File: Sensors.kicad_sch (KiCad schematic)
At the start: 7 parts, among them U1 ICM-42670-P, U401 MPU-6050

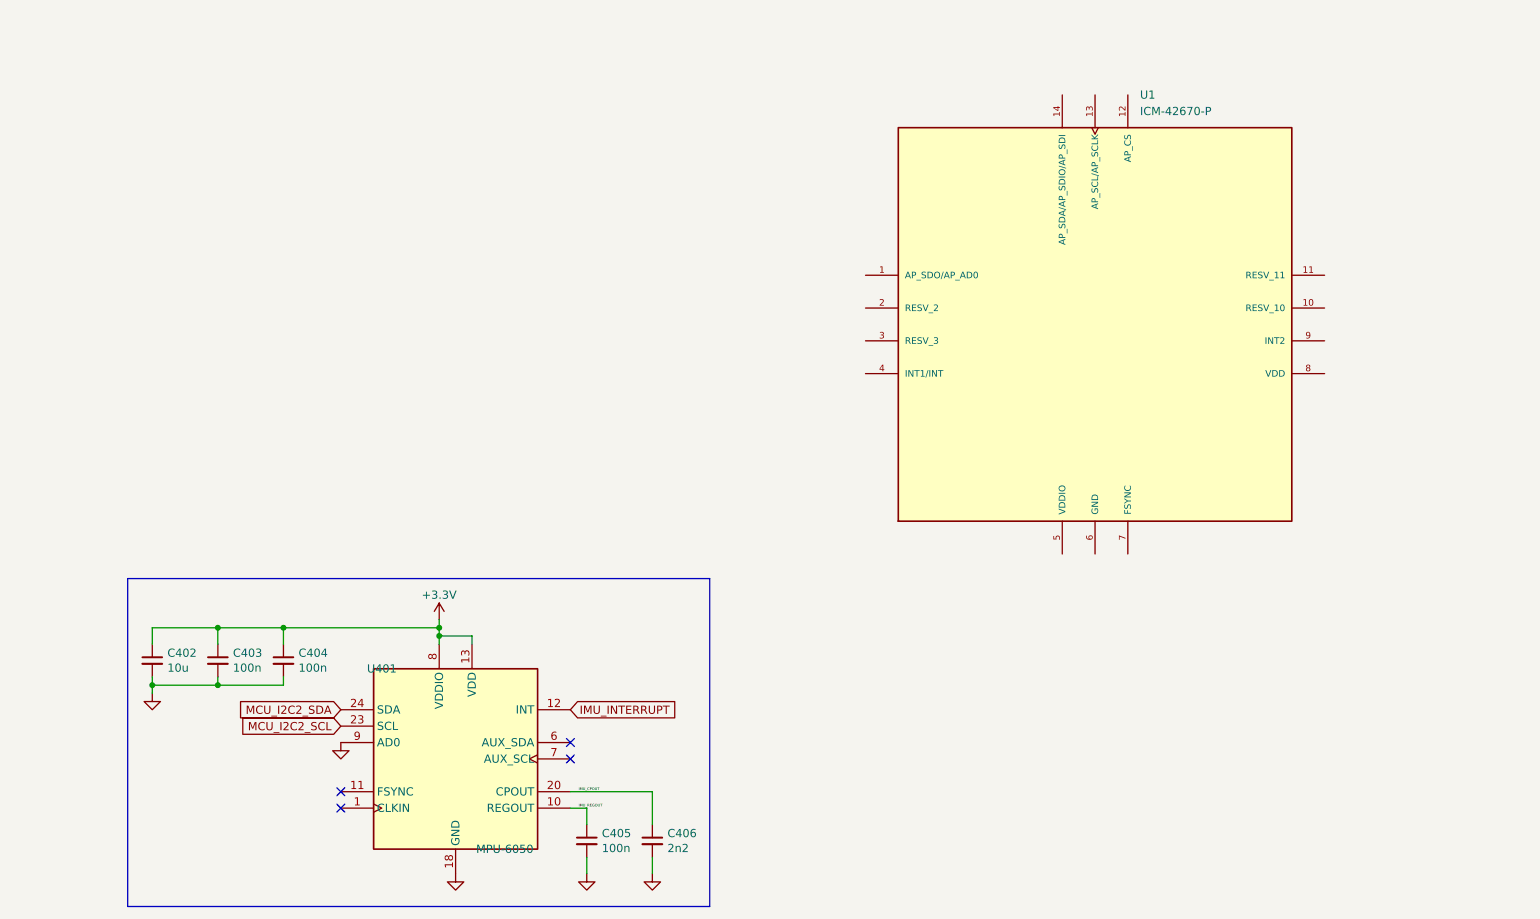
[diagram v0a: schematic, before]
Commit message: replaced CAN transceiver, introduced new IMU
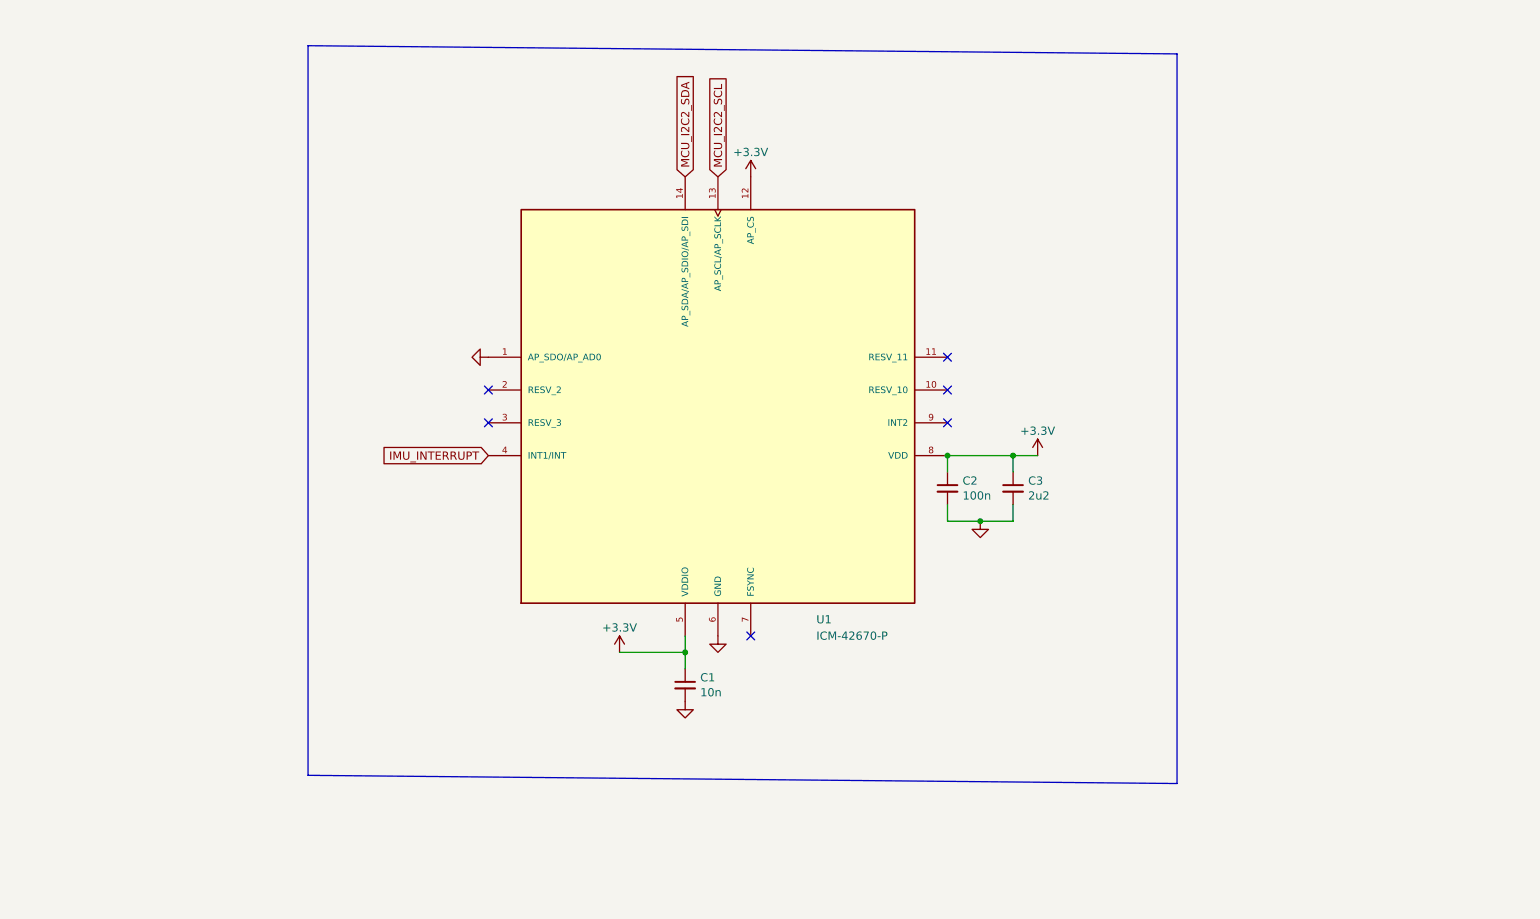
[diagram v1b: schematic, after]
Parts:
- removed C402: 10u, Capacitor_SMD:C_0603_1608Metric, symbol Device:C_Small
- removed C403, C404, C405: 100n, Capacitor_SMD:C_0402_1005Metric, symbol Device:C_Small
- removed C406: 2n2, Capacitor_SMD:C_0402_1005Metric, symbol Device:C_Small
- removed U401: MPU-6050, Sensor_Motion:InvenSense_QFN-24_4x4mm_P0.5mm, symbol Sensor_Motion:MPU-6050
- added C1: 10n, Capacitor_SMD:C_0402_1005Metric, symbol Device:C_Small
- added C2: 100n, Capacitor_SMD:C_0402_1005Metric, symbol Device:C_Small
- added C3: 2u2, Capacitor_SMD:C_0402_1005Metric, symbol Device:C_Small
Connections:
- net +3V3: now also U1.12 (AP_CS), U1.5 (VDDIO), U1.8 (VDD), C1.1, C2.1, C3.1
- net GND: now also U1.1 (AP_SDO/AP_AD0), U1.6 (GND), C1.2, C2.2, C3.2
- net IMU_INTERRUPT: now also U1.4 (INT1/INT)
- net MCU_I2C2_SCL: now also U1.13 (AP_SCL/AP_SCLK)
- net MCU_I2C2_SDA: now also U1.14 (AP_SDA/AP_SDIO/AP_SDI)
- no-connect marks 4 -> 6
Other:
- moved on the sheet: U1

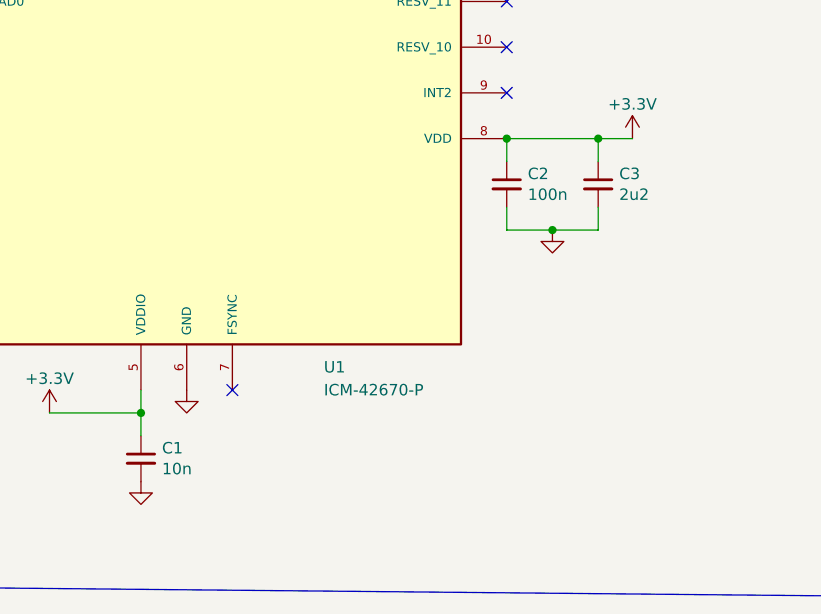
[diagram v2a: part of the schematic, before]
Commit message: gpio breakout stuff
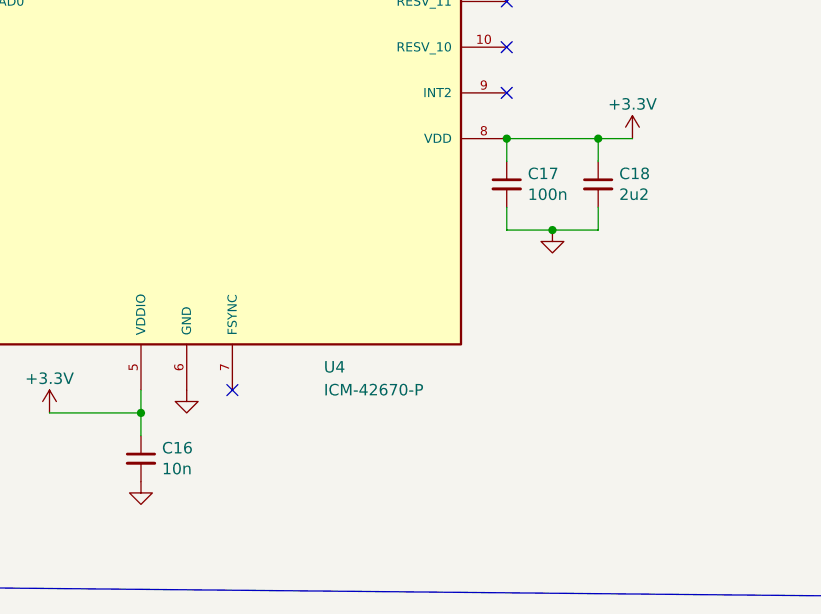
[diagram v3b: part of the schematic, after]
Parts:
- renumbered C1 to C16, C2 to C17, C3 to C18, U1 to U4
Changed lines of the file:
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@@
   (symbol (lib_id "Device:C_Small") (at 175.26 97.79 0) (unit 1)
     (in_bom yes) (on_board yes)
-    (property "Reference" "C2" (id 0) (at 177.5968 96.6216 0)
+    (property "Reference" "C17" (id 0) (at 177.5968 96.6216 0)
       (effects (font (size 1.27 1.27)) (justify left))
     )
@@
   (symbol (lib_id "Device:C_Small") (at 134.62 128.27 0) (unit 1)
     (in_bom yes) (on_board yes)
-    (property "Reference" "C1" (id 0) (at 136.9568 127.1016 0)
+    (property "Reference" "C16" (id 0) (at 136.9568 127.1016 0)
       (effects (font (size 1.27 1.27)) (justify left))
     )
@@
   (symbol (lib_id "power:GND") (at 180.34 102.87 0) (unit 1)
     (in_bom yes) (on_board yes)
-    (property "Reference" "#PWR030" (id 0) (at 180.34 109.22 0)
+    (property "Reference" "#PWR041" (id 0) (at 180.34 109.22 0)
       (effects (font (size 1.27 1.27)) hide)
     )
@@
   (symbol (lib_id "BluePhil-rescue:+3.3V-power") (at 124.46 123.19 0) (unit 1)
     (in_bom yes) (on_board yes)
-    (property "Reference" "#PWR05" (id 0) (at 124.46 127 0)
+    (property "Reference" "#PWR037" (id 0) (at 124.46 127 0)
       (effects (font (size 1.27 1.27)) hide)
     )
@@
   (symbol (lib_id "ICM-42670-P:ICM-42670-P") (at 139.7 85.09 0) (unit 1)
     (in_bom yes) (on_board yes)
-    (property "Reference" "U1" (id 0) (at 154.94 118.11 0)
+    (property "Reference" "U4" (id 0) (at 154.94 118.11 0)
       (effects (font (size 1.27 1.27)) (justify left))
     )
@@
   (symbol (lib_id "BluePhil-rescue:+3.3V-power") (at 144.78 49.53 0) (unit 1)
     (in_bom yes) (on_board yes)
-    (property "Reference" "#PWR014" (id 0) (at 144.78 53.34 0)
+    (property "Reference" "#PWR040" (id 0) (at 144.78 53.34 0)
       (effects (font (size 1.27 1.27)) hide)
     )
@@
   (symbol (lib_id "Device:C_Small") (at 185.42 97.79 0) (unit 1)
     (in_bom yes) (on_board yes)
-    (property "Reference" "C3" (id 0) (at 187.7568 96.6216 0)
+    (property "Reference" "C18" (id 0) (at 187.7568 96.6216 0)
       (effects (font (size 1.27 1.27)) (justify left))
     )
@@
   (symbol (lib_id "power:GND") (at 139.7 120.65 0) (unit 1)
     (in_bom yes) (on_board yes)
-    (property "Reference" "#PWR010" (id 0) (at 139.7 127 0)
+    (property "Reference" "#PWR039" (id 0) (at 139.7 127 0)
       (effects (font (size 1.27 1.27)) hide)
     )
@@
   (symbol (lib_id "BluePhil-rescue:+3.3V-power") (at 189.23 92.71 0) (unit 1)
     (in_bom yes) (on_board yes)
-    (property "Reference" "#PWR031" (id 0) (at 189.23 96.52 0)
+    (property "Reference" "#PWR042" (id 0) (at 189.23 96.52 0)
       (effects (font (size 1.27 1.27)) hide)
     )
@@
   (symbol (lib_id "power:GND") (at 134.62 130.81 0) (unit 1)
     (in_bom yes) (on_board yes)
-    (property "Reference" "#PWR07" (id 0) (at 134.62 137.16 0)
+    (property "Reference" "#PWR038" (id 0) (at 134.62 137.16 0)
       (effects (font (size 1.27 1.27)) hide)
     )
@@
   (symbol (lib_id "power:GND") (at 104.14 77.47 270) (unit 1)
     (in_bom yes) (on_board yes)
-    (property "Reference" "#PWR02" (id 0) (at 97.79 77.47 0)
+    (property "Reference" "#PWR036" (id 0) (at 97.79 77.47 0)
       (effects (font (size 1.27 1.27)) hide)
     )

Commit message: skgnigniogni
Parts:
- added J4: BM04B-SURS-TFLFSN, SnapEDA Library:JST_BM04B-SURS-TF(LF)(SN), symbol BM04B:BM04B-SURS-TFLFSN
- added JP1, JP2: SolderJumper_3_Bridged12, Jumper:SolderJumper-3_P1.3mm_Bridged12_Pad1.0x1.5mm, symbol Jumper:SolderJumper_3_Bridged12
- added R17, R18: 0R, Resistor_SMD:R_0402_1005Metric, symbol Device:R_Small
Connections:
- net +3V3: now also JP1.1 (A), JP2.3 (B)
- net GND: now also JP1.3 (B), JP2.1 (A)
- new net: J4.2, R17.2
- new net: J4.4, JP2.2 (C)
- new net: J4.1, JP1.2 (C)
- new net: J4.3, R18.2
- new net MCU_I2C1_SCL: R18.1
- new net MCU_I2C1_SDA: R17.1
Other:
- moved on the sheet: C16, C17, C18, U4

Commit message: WEBGIOWEBGIOBWEG
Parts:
- C402: renamed from C17; value 100n -> 0.1u
- renumbered C16 to C401, C18 to C403, J4 to J401, JP1 to JP401, JP2 to JP402, R17 to R401, R18 to R402, U4 to U401
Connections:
- net GND: now also U401.7 (FSYNC)
- no-connect marks 6 -> 5
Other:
- note added: "Caps are X7R"
- note added: "Encoder board connector"
- note added: "IMU/Temperature"
- moved on the sheet: C401, JP402

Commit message: final commit before holiday
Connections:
- net MCU_I2C1_SCL: now also U401.13 (AP_SCL/AP_SCLK); no longer R402.1
- net MCU_I2C1_SDA: now also U401.14 (AP_SDA/AP_SDIO/AP_SDI); no longer R401.1
- net MCU_I2C2_SCL: now also R402.1; no longer U401.13 (AP_SCL/AP_SCLK)
- net MCU_I2C2_SDA: now also R401.1; no longer U401.14 (AP_SDA/AP_SDIO/AP_SDI)
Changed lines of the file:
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@@
     )
   )
-  (global_label "MCU_I2C1_SCL" (shape input) (at 199.39 52.07 180) (fields_autoplaced)
+  (global_label "MCU_I2C2_SDA" (shape input) (at 199.39 49.53 180) (fields_autoplaced)
     (effects (font (size 1.27 1.27)) (justify right))
-    (property "Intersheet References" "${INTERSHEET_REFS}" (id 0) (at 183.2772 51.9906 0)
-      (effects (font (size 1.27 1.27)) (justify right) hide)
-    )
-  )
-  (global_label "MCU_I2C1_SDA" (shape input) (at 199.39 49.53 180) (fields_autoplaced)
-    (effects (font (size 1.27 1.27)) (justify right))
-    (property "Intersheet References" "${INTERSHEET_REFS}" (id 0) (at 183.2168 49.4506 0)
-      (effects (font (size 1.27 1.27)) (justify right) hide)
-    )
-  )
-  (global_label "MCU_I2C2_SDA" (shape input) (at 88.9 48.26 90) (fields_autoplaced)
-    (effects (font (size 1.27 1.27)) (justify left))
-    (property "Intersheet References" "${INTERSHEET_REFS}" (id 0) (at 204.47 -93.98 0)
+    (property "Intersheet References" "${INTERSHEET_REFS}" (id 0) (at 57.15 -66.04 0)
       (effects (font (size 1.27 1.27)) hide)
     )
   )
-  (global_label "MCU_I2C2_SCL" (shape input) (at 93.98 48.26 90) (fields_autoplaced)
+  (global_label "MCU_I2C1_SCL" (shape input) (at 93.98 48.26 90) (fields_autoplaced)
     (effects (font (size 1.27 1.27)) (justify left))
-    (property "Intersheet References" "${INTERSHEET_REFS}" (id 0) (at 212.09 -93.98 0)
+    (property "Intersheet References" "${INTERSHEET_REFS}" (id 0) (at 94.0594 32.1472 90)
+      (effects (font (size 1.27 1.27)) (justify left) hide)
+    )
+  )
+  (global_label "MCU_I2C1_SDA" (shape input) (at 88.9 48.26 90) (fields_autoplaced)
+    (effects (font (size 1.27 1.27)) (justify left))
+    (property "Intersheet References" "${INTERSHEET_REFS}" (id 0) (at 88.9794 32.0868 90)
+      (effects (font (size 1.27 1.27)) (justify left) hide)
+    )
+  )
+  (global_label "MCU_I2C2_SCL" (shape input) (at 199.39 52.07 180) (fields_autoplaced)
+    (effects (font (size 1.27 1.27)) (justify right))
+    (property "Intersheet References" "${INTERSHEET_REFS}" (id 0) (at 57.15 -66.04 0)
       (effects (font (size 1.27 1.27)) hide)
     )

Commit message: isegniosndg
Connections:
- net MCU_I2C1_SCL renamed MCU_I2C3_SCL
- net MCU_I2C1_SDA renamed MCU_I2C3_SDA
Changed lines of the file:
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@@
     )
   )
-  (global_label "MCU_I2C1_SCL" (shape input) (at 93.98 48.26 90) (fields_autoplaced)
+  (global_label "MCU_I2C3_SCL" (shape input) (at 93.98 48.26 90) (fields_autoplaced)
     (effects (font (size 1.27 1.27)) (justify left))
-    (property "Intersheet References" "${INTERSHEET_REFS}" (id 0) (at 94.0594 32.1472 90)
+    (property "Intersheet References" "${INTERSHEET_REFS}" (id 0) (at 93.9006 32.1472 90)
       (effects (font (size 1.27 1.27)) (justify left) hide)
     )
   )
-  (global_label "MCU_I2C1_SDA" (shape input) (at 88.9 48.26 90) (fields_autoplaced)
+  (global_label "MCU_I2C3_SDA" (shape input) (at 88.9 48.26 90) (fields_autoplaced)
     (effects (font (size 1.27 1.27)) (justify left))
-    (property "Intersheet References" "${INTERSHEET_REFS}" (id 0) (at 88.9794 32.0868 90)
+    (property "Intersheet References" "${INTERSHEET_REFS}" (id 0) (at 88.8206 32.0868 90)
       (effects (font (size 1.27 1.27)) (justify left) hide)
     )

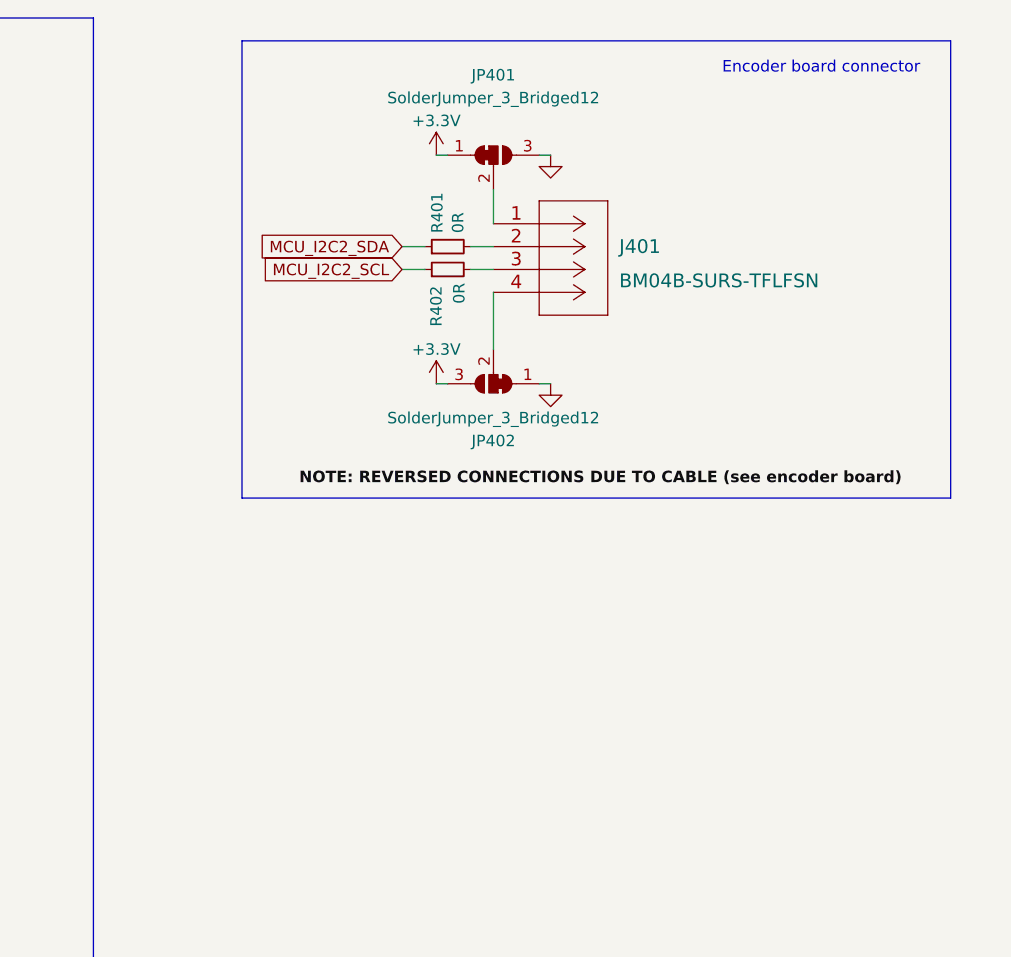
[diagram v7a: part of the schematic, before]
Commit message: First draft routing
Separated into shield and main board projects
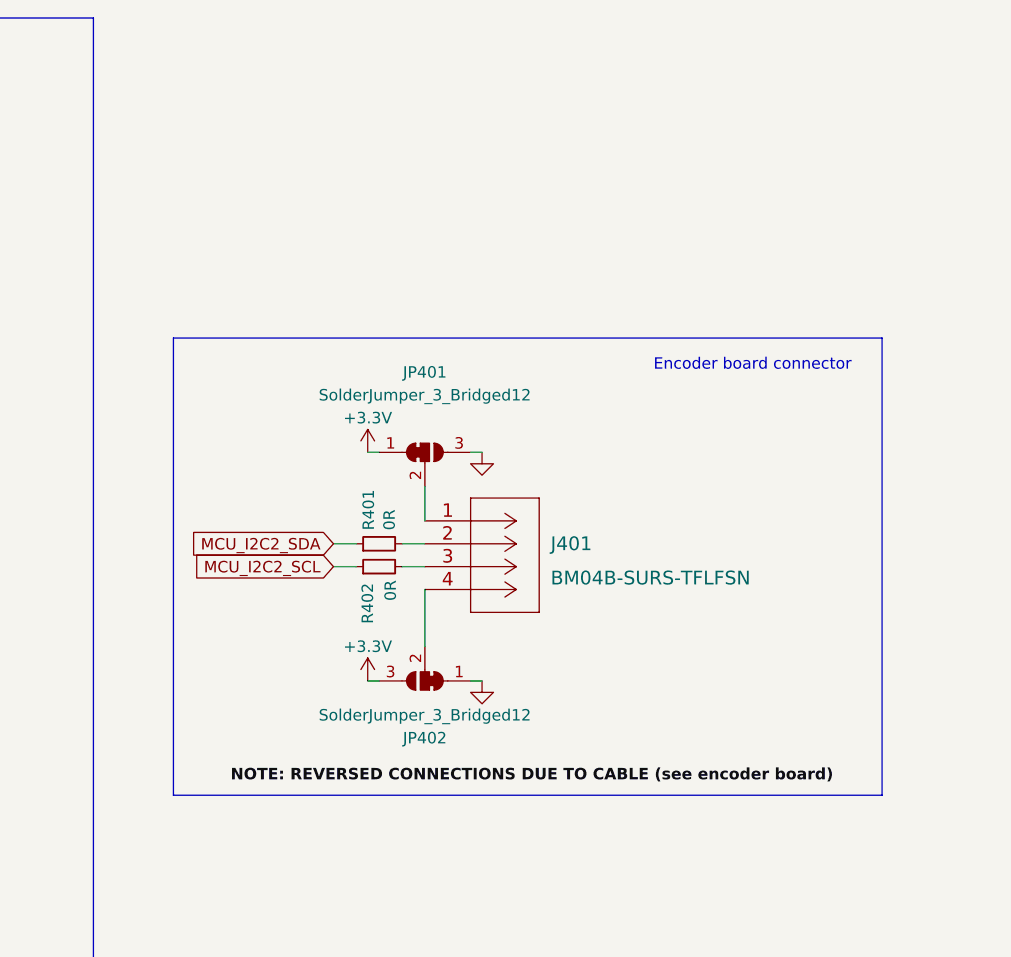
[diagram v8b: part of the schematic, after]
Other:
- moved on the sheet: J401, JP401, JP402, R401, R402
